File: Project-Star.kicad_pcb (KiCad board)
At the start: 2 copper layers, 17 parts, among them Q1 CSD13380F3, Q2 CSD13380F3, Q3 CSD13380F3, Q4 CSD13380F3, Q5 CSD13380F3, Q6 CSD13380F3, Q7 CSD13380F3, Q8 CSD13380F3, Q9 2N7002E, U1 BQ7693000DBT, U2 BQ78350DBT-R1, U3 BQ76200PW, U4 MSP430G2755IDA38, U5 MSP430G2553IPW20

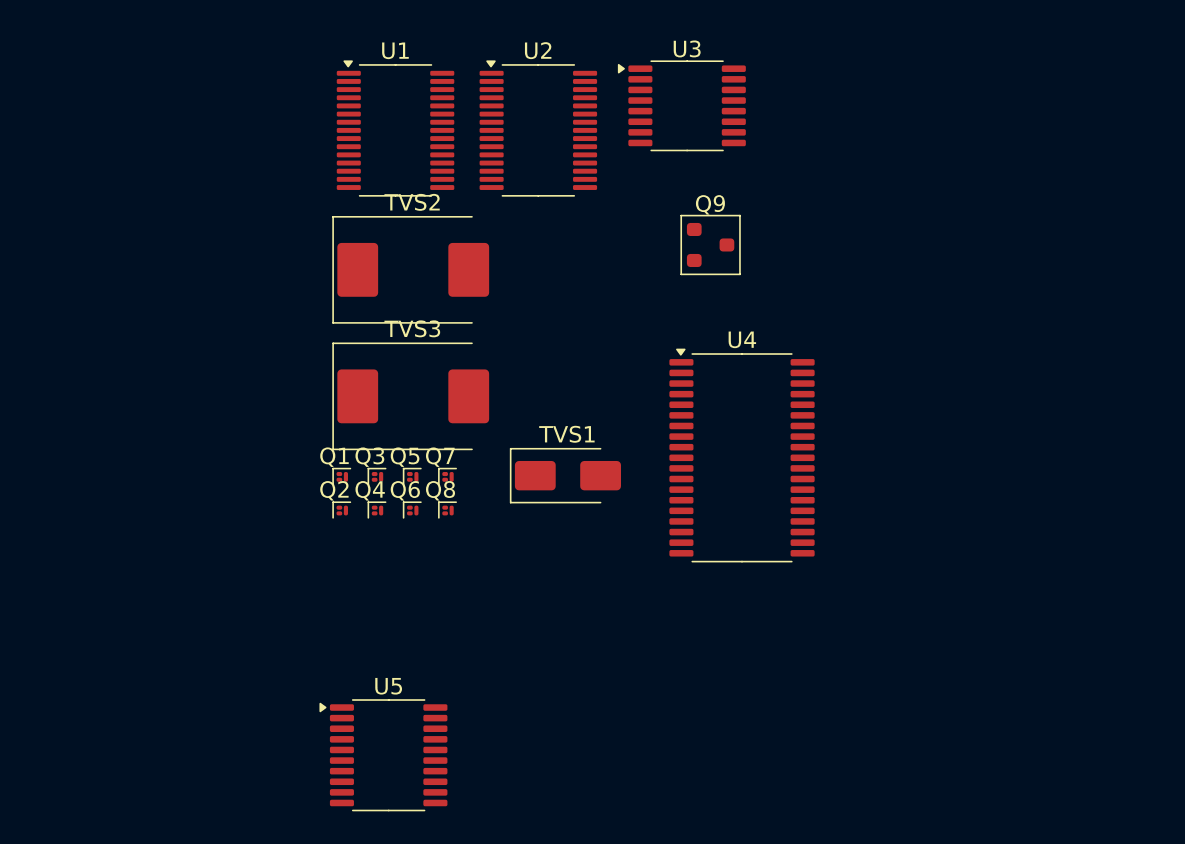
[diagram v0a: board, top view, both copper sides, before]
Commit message: cgr, dsg fets + jtag
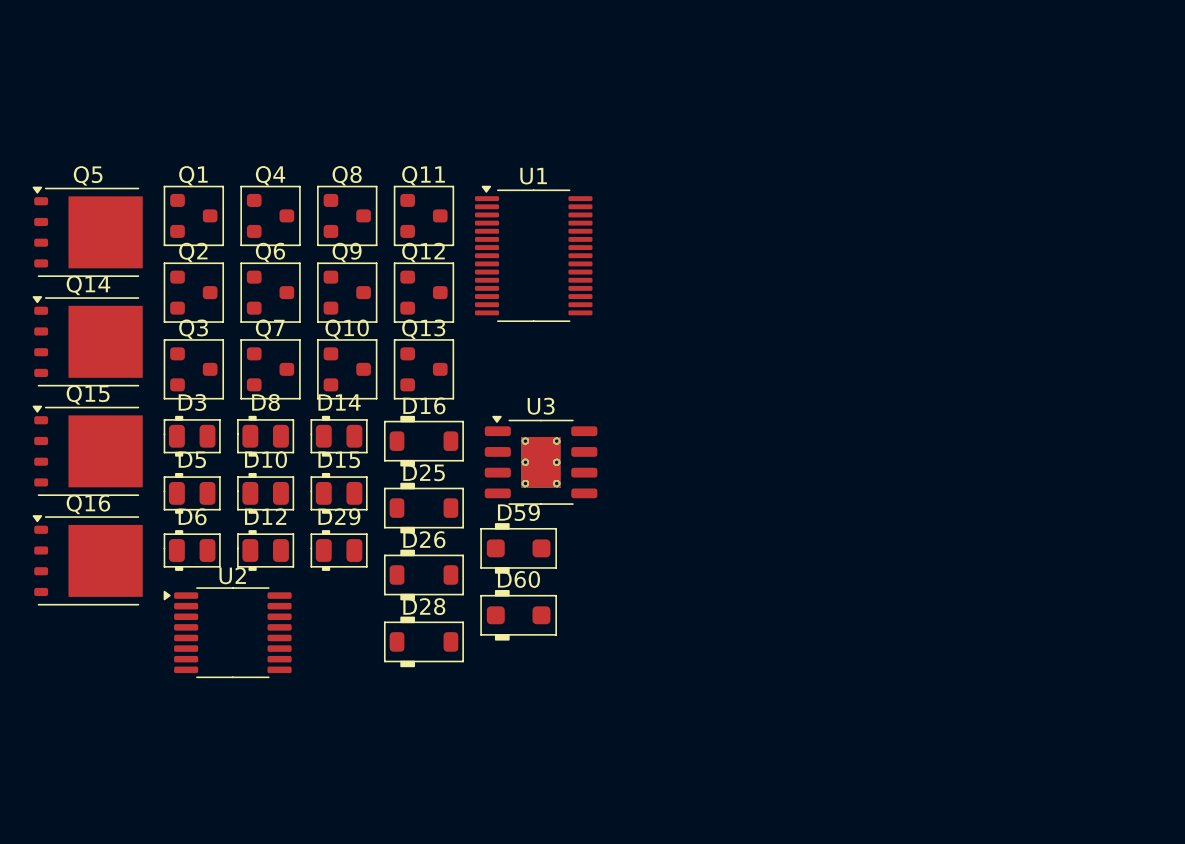
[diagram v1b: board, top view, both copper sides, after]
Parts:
- removed TVS1: SMAJ40A, Diode_SMD:D_SMA
- removed TVS2, TVS3: 5.0SMDJ36A, Diode_SMD:D_SMC
- removed U4: MSP430G2755IDA38, Package_SO:TSSOP-38_6.1x12.5mm_P0.65mm
- removed U5: MSP430G2553IPW20, Package_SO:TSSOP-20_4.4x6.5mm_P0.65mm
- added D10: LED, PCM_Diode_SMD_AKL:D_0805_2012Metric, F.Cu at (128.6, 99.5)
- added D12: LED, PCM_Diode_SMD_AKL:D_0805_2012Metric, F.Cu at (128.6, 103.0)
- added D14: LED, PCM_Diode_SMD_AKL:D_0805_2012Metric, F.Cu at (133.1, 96.0)
- added D15: LED, PCM_Diode_SMD_AKL:D_0805_2012Metric, F.Cu at (133.1, 99.5)
- added D16: 1N4148W, PCM_Diode_SMD_AKL:D_SOD-123, F.Cu at (138.3, 96.3)
- added D25: 1N4148W, PCM_Diode_SMD_AKL:D_SOD-123, F.Cu at (138.3, 100.4)
- added D26: 1N4148W, PCM_Diode_SMD_AKL:D_SOD-123, F.Cu at (138.3, 104.5)
- added D28: 1N4148W, PCM_Diode_SMD_AKL:D_SOD-123, F.Cu at (138.3, 108.6)
- added D29: LED, PCM_Diode_SMD_AKL:D_0805_2012Metric, F.Cu at (133.1, 103.0)
- added D3: LED, PCM_Diode_SMD_AKL:D_0805_2012Metric, F.Cu at (124.1, 96.0)
- added D5: LED, PCM_Diode_SMD_AKL:D_0805_2012Metric, F.Cu at (124.1, 99.5)
- added D59: PTVS40VS1UTR, PCM_Diode_SMD_AKL:D_SOD-123F, F.Cu at (144.1, 102.9)
- added D6: LED, PCM_Diode_SMD_AKL:D_0805_2012Metric, F.Cu at (124.1, 103.0)
- added D60: PTVS40VS1UTR, PCM_Diode_SMD_AKL:D_SOD-123F, F.Cu at (144.1, 107.0)
- added D8: LED, PCM_Diode_SMD_AKL:D_0805_2012Metric, F.Cu at (128.6, 96.0)
- added Q10: ZXMP10A13F, PCM_Package_TO_SOT_SMD_AKL:SOT-23, F.Cu at (133.6, 91.9)
- added Q11: ZXMP10A13F, PCM_Package_TO_SOT_SMD_AKL:SOT-23, F.Cu at (138.3, 82.5)
- added Q12: BSS123, PCM_Package_TO_SOT_SMD_AKL:SOT-23, F.Cu at (138.3, 87.2)
- added Q13: ZXMP10A13F, PCM_Package_TO_SOT_SMD_AKL:SOT-23, F.Cu at (138.3, 91.9)
- added Q14: CSD19531Q5A, Package_TO_SOT_SMD:TDSON-8-1, F.Cu at (117.7, 90.2)
- added Q15: CSD19531Q5A, Package_TO_SOT_SMD:TDSON-8-1, F.Cu at (117.7, 97.0)
- added Q16: CSD19531Q5A, Package_TO_SOT_SMD:TDSON-8-1, F.Cu at (117.7, 103.7)
- Q1, Q2, Q3, Q4, Q6, Q7, Q8: value CSD13380F3 -> DMN2004K; footprint Package_DFN_QFN:Texas_PicoStar_DFN-3_0.69x0.60mm -> PCM_Package_TO_SOT_SMD_AKL:SOT-23
- Q5: value CSD13380F3 -> CSD19531Q5A; footprint Package_DFN_QFN:Texas_PicoStar_DFN-3_0.69x0.60mm -> Package_TO_SOT_SMD:TDSON-8-1
- Q9: value 2N7002E -> DMN2004K
- U1: value BQ7693000DBT -> BQ7693006DBTR
- U2: value BQ78350DBT-R1 -> BQ76200PW; footprint Package_SO:TSSOP-30_4.4x7.8mm_P0.5mm -> Package_SO:TSSOP-16_4.4x5mm_P0.65mm
- U3: value BQ76200PW -> LM5164DDA; footprint Package_SO:TSSOP-16_4.4x5mm_P0.65mm -> Package_SO:HSOP-8-1EP_3.9x4.9mm_P1.27mm_EP2.41x3.1mm_ThermalVias
- moved U2 36.0 mm to (126.6, 108.1)
- moved Q5 24.9 mm to (117.7, 83.5)
- moved U3 23.6 mm to (145.5, 97.6)
- moved Q9 22.5 mm to (133.6, 87.2)
- moved Q4 19.2 mm to (128.9, 82.5)
- moved Q8 19.1 mm to (133.6, 82.5)
- moved Q1 18.4 mm to (124.2, 82.5)
- moved Q2 16.2 mm to (124.2, 87.2)
- moved Q6 15.9 mm to (128.9, 87.2)
- moved Q3 13.0 mm to (124.2, 91.9)
- moved Q7 12.7 mm to (128.9, 91.9)
- moved U1 11.4 mm to (145.0, 85.0)
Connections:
- net /ALERT renamed Net-(U1-ALERT)
- net /CP_EN renamed Net-(U3-FB)
- net /PCHG_EN renamed Net-(U3-SW)
- net /PMON_EN renamed Net-(U3-BST)
- net /REGOUT renamed +3V3
- net BAT- renamed /C0
- net C5 renamed Net-(D13-A)
- net Net-(U1-CAP1) renamed /CAP1
- net Net-(U1-CAP2) renamed /CAP2
- net Net-(U1-SRN) renamed /SRN
- net Net-(U1-SRP) renamed /SRP
- net Net-(U1-TS2) renamed /TS2
- net Net-(U1-VC0) renamed /VC0
- net Net-(U1-VC1) renamed /VC1
- net Net-(U1-VC2) renamed /VC2
- net Net-(U1-VC3) renamed /VC3
- net Net-(U1-VC5B) renamed /VC5B
- net Net-(U1-VC6) renamed /VC5
- net Net-(U1-VC7) renamed /VC6
- net Net-(U1-VC8) renamed /VC7
- Q2 pad 2: C1 -> /C1
- Q3 pad 2: C2 -> /C2
- Q4 pad 2: C3 -> /C3
- Q5 pad 1: Net-(D5-K) -> BATT+
- Q5 pad 2: C4 -> BATT+
- Q5 pad 3: Net-(Q5-D) -> BATT+
- Q7 pad 2: C7 -> /C7
- Q8 pad 2: C6 -> /C6
- Q9 pad 2: /REGSRC -> /C5
- U1 pad 1: /DSG_EN -> /DSG
- U1 pad 10: /VCX5 -> /VC5X
- U1 pad 15: /VCX5 -> /BAT
- U1 pad 16: Net-(D9-A) -> /VC8
- U1 pad 2: /CHG_EN -> /CHG
- U1 pad 22: Net-(D10-A) -> /VC4
- U2 pad 1: unconnected-(U2-COM-Pad1) -> Net-(U2-VDDCP)
- U2 pad 11: unconnected-(U2-SMBD-Pad11) -> Net-(U2-PACK)
- U2 pad 12: unconnected-(U2-VEN-Pad12) -> Net-(U2-DSG)
- U2 pad 14: unconnected-(U2-~{DISP}-Pad14) -> /PCHG
- U2 pad 16: unconnected-(U2-LED1-Pad16) -> Net-(U2-CHG)
- U2 pad 2: unconnected-(U2-ALERT-Pad2) -> /U_BAT
- U2 pad 4: unconnected-(U2-SCL-Pad4) -> Net-(U2-CHG_EN)
- U2 pad 5: unconnected-(U2-~{PRECHG}-Pad5) -> Net-(U2-CP_EN)
- U2 pad 6: unconnected-(U2-VAUX-Pad6) -> Net-(U2-DSG_EN)
- U2 pad 7: unconnected-(U2-BAT-Pad7) -> GND
- U2 pad 8: unconnected-(U2-~{PRES}-Pad8) -> Net-(U2-PCHG_EN)
- U2 pad 9: unconnected-(U2-~{KEYIN}-Pad9) -> GND
- U3 pad 1: /VDDCP -> GND
- U3 pad 2: /BAT -> Net-(Q11-D)
- U3 pad 3: unconnected-(U3-NC-Pad3) -> Net-(Q11-D)
- U3 pad 4: /CHG_EN -> Net-(U3-RON)
- U3 pad 6: /DSG_EN -> unconnected-(U3-PGOOD-Pad6)

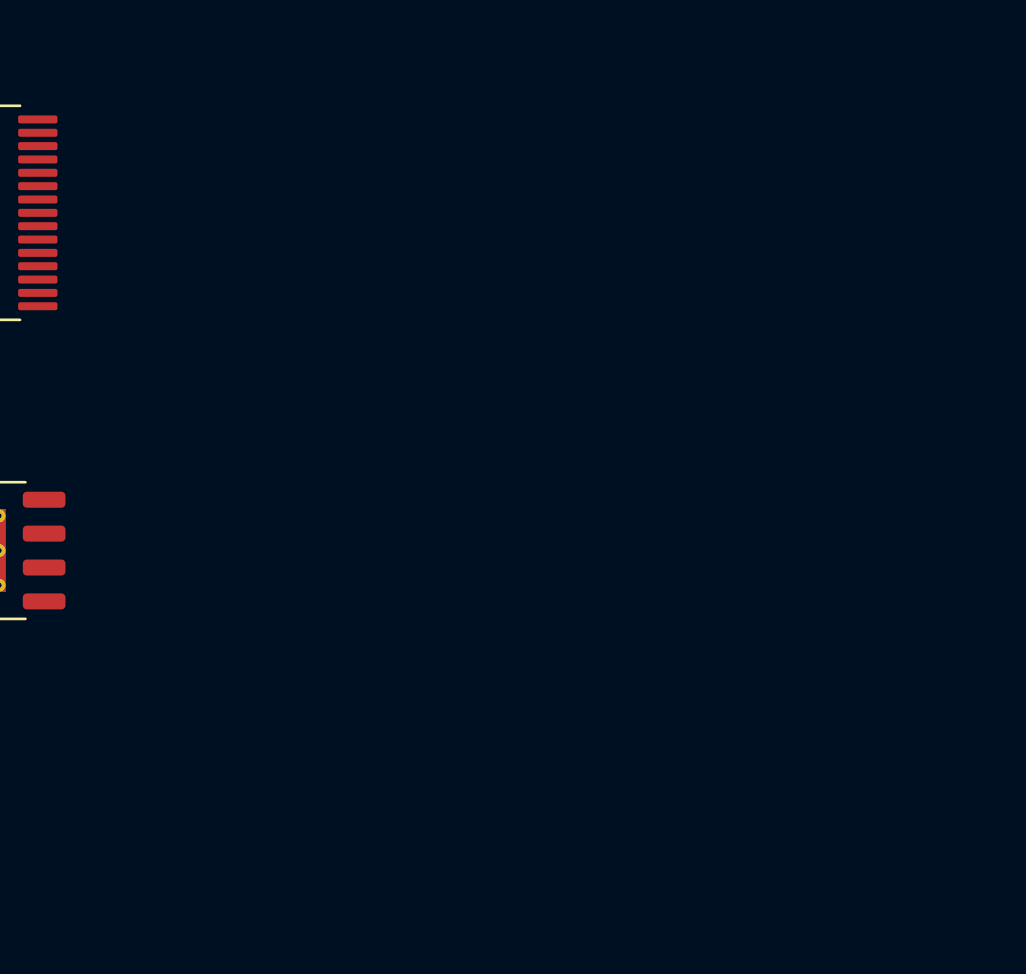
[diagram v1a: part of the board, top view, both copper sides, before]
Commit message: commit before simplifying and removing features
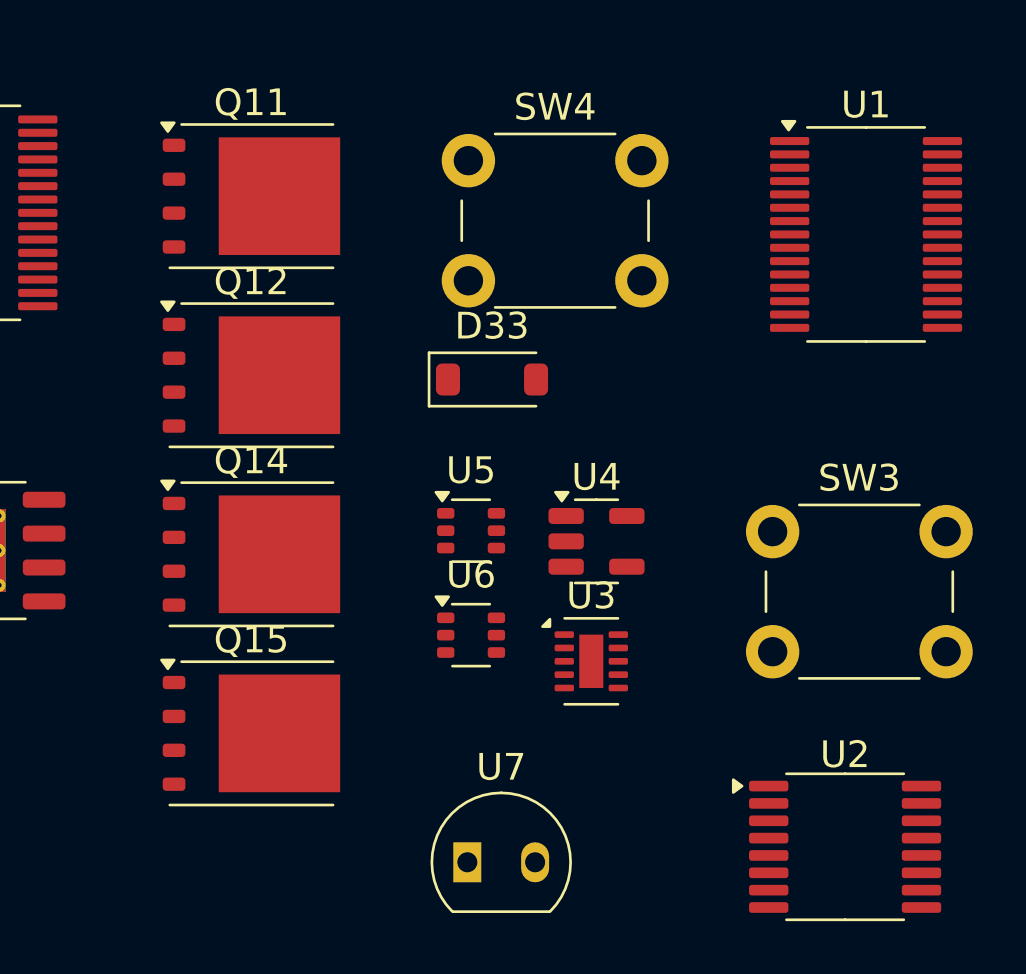
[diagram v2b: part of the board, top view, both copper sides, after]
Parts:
- added D33: MBR0520LT, Diode_SMD:D_SOD-123, F.Cu at (164.9, 91.2)
- added Q11: CSD19531Q5A, Package_TO_SOT_SMD:TDSON-8-1, F.Cu at (155.9, 84.3)
- added Q12: CSD19531Q5A, Package_TO_SOT_SMD:TDSON-8-1, F.Cu at (155.9, 91.1)
- added Q14: CSD19531Q5A, Package_TO_SOT_SMD:TDSON-8-1, F.Cu at (155.9, 97.8)
- added Q15: CSD19531Q5A, Package_TO_SOT_SMD:TDSON-8-1, F.Cu at (155.9, 104.5)
- added SW3: Push_Button, Button_Switch_THT:SW_PUSH_6mm, F.Cu at (175.4, 96.9)
- added SW4: Push_Button, Button_Switch_THT:SW_PUSH_6mm, F.Cu at (164.0, 83.0)
- added U1: BQ7693006DBTR, Package_SO:TSSOP-30_4.4x7.8mm_P0.5mm, F.Cu at (178.9, 85.8)
- added U2: BQ76200PW, Package_SO:TSSOP-16_4.4x5mm_P0.65mm, F.Cu at (178.1, 108.7)
- added U3: MAX17502EATB+T, Package_DFN_QFN:TDFN-10-1EP_2x3mm_P0.5mm_EP0.9x2mm, F.Cu at (168.6, 101.8)
- added U4: TLV75733PDBV, Package_TO_SOT_SMD:SOT-23-5, F.Cu at (168.8, 97.3)
- added U5: LM66100DCKR, Package_TO_SOT_SMD:SOT-363_SC-70-6, F.Cu at (164.1, 96.9)
- added U6: LM66100DCKR, Package_TO_SOT_SMD:SOT-363_SC-70-6, F.Cu at (164.1, 100.8)
- added U7: LMT01LPG, Package_TO_SOT_THT:TO-92-2, F.Cu at (164.0, 109.3)
